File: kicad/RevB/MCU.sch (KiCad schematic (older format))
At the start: 12 parts, among them SW1 SW_SPDT, SW2 SW_SPST, U2 SE8233X2, U3 STM32F051K4Tx

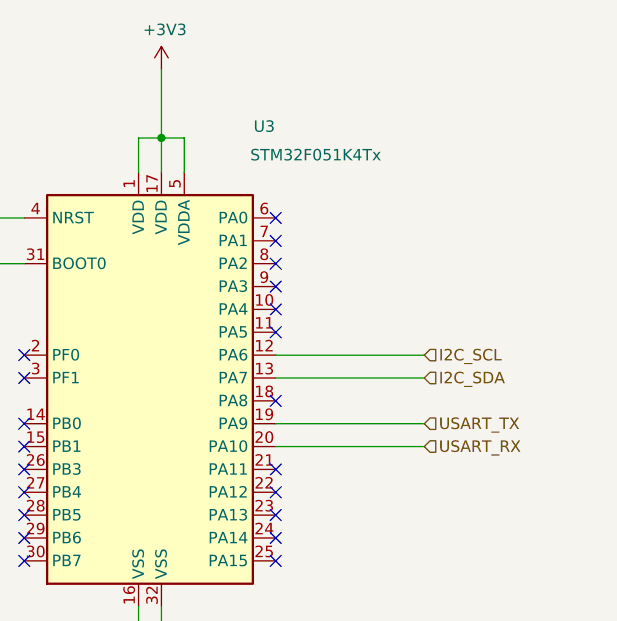
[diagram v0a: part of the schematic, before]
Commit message: updated revb hw
- Added pull up resistors to i2C bus (allows direct connection to mcu from oled port)
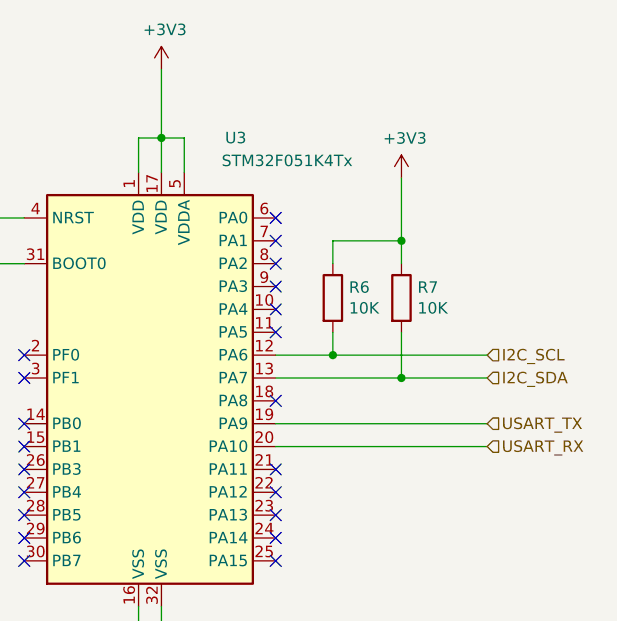
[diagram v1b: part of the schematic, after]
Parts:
- added R6, R7: 10K, Resistor_SMD:R_0805_2012Metric_Pad1.15x1.40mm_HandSolder, symbol Device:R
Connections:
- net +3V3: now also R6.1, R7.1
- net I2C_SCL: now also R6.2
- net I2C_SDA: now also R7.2
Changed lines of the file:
@@
 $EndDescr
 Wire Wire Line
-	7800 3725 8450 3725
-Wire Wire Line
-	7800 3625 8450 3625
-Wire Wire Line
-	7800 3325 8450 3325
-Wire Wire Line
-	7800 3425 8450 3425
+	7800 3725 8725 3725
+Wire Wire Line
+	7800 3625 8725 3625
+Wire Wire Line
+	7800 3325 8050 3325
+Wire Wire Line
+	7800 3425 8350 3425
 NoConn ~ 7800 3525
 NoConn ~ 7800 3225
@@
 NoConn ~ 7800 3925
 NoConn ~ 7800 4225
-Text HLabel 8450 3325 2    50   Input ~ 0
+Text HLabel 8725 3325 2    50   Input ~ 0
 I2C_SCL
-Text HLabel 8450 3425 2    50   Input ~ 0
+Text HLabel 8725 3425 2    50   Input ~ 0
 I2C_SDA
-Text HLabel 8450 3625 2    50   Input ~ 0
+Text HLabel 8725 3625 2    50   Input ~ 0
 USART_TX
-Text HLabel 8450 3725 2    50   Input ~ 0
+Text HLabel 8725 3725 2    50   Input ~ 0
 USART_RX
 $Comp
@@
 AR Path="/5F6E45CF" Ref="U?"  Part="1"
 AR Path="/5F6E342E/5F6E45CF" Ref="U3"  Part="1"
-F 0 "U3" H 7750 4525 50  0000 C CNN
-F 1 "STM32F051K4Tx" H 7975 4400 50  0000 C CNN
+F 0 "U3" H 7625 4475 50  0000 C CNN
+F 1 "STM32F051K4Tx" H 7850 4375 50  0000 C CNN
 F 2 "Package_QFP:LQFP-32_7x7mm_P0.8mm" H 6800 2525 50  0001 R CNN
 F 3 "http://www.st.com/st-web-ui/static/active/en/resource/technical/document/datasheet/DM00039193.pdf" H 7300 3425 50  0001 C CNN
@@
 Text Notes 5550 2175 0    50   ~ 0
 Tactile SPST salvaged\nfrom an old nano clone
+$Comp
+L Device:R R6
+U 1 1 5F70F57E
+P 8050 3075
+F 0 "R6" H 8120 3121 50  0000 L CNN
+F 1 "10K" H 8120 3030 50  0000 L CNN
+F 2 "Resistor_SMD:R_0805_2012Metric_Pad1.15x1.40mm_HandSolder" V 7980 3075 50  0001 C CNN
+F 3 "~" H 8050 3075 50  0001 C CNN
+	1    8050 3075
+	1    0    0    -1
+$EndComp
+$Comp
+L Device:R R7
+U 1 1 5F70FAD9
+P 8350 3075
+F 0 "R7" H 8420 3121 50  0000 L CNN
+F 1 "10K" H 8420 3030 50  0000 L CNN
+F 2 "Resistor_SMD:R_0805_2012Metric_Pad1.15x1.40mm_HandSolder" V 8280 3075 50  0001 C CNN
+F 3 "~" H 8350 3075 50  0001 C CNN
+	1    8350 3075
+	1    0    0    -1
+$EndComp
+$Comp
+L power:+3V3 #PWR?
+U 1 1 5F711644
+P 8350 2550
+AR Path="/5F711644" Ref="#PWR?"  Part="1"
+AR Path="/5F6E342E/5F711644" Ref="#PWR021"  Part="1"
+F 0 "#PWR021" H 8350 2400 50  0001 C CNN
+F 1 "+3V3" H 8365 2723 50  0000 C CNN
+F 2 "" H 8350 2550 50  0001 C CNN
+F 3 "" H 8350 2550 50  0001 C CNN
+	1    8350 2550
+	1    0    0    -1
+$EndComp
+Wire Wire Line
+	8350 2550 8350 2825
+Wire Wire Line
+	8350 2825 8050 2825
+Wire Wire Line
+	8050 2825 8050 2925
+Connection ~ 8350 2825
+Wire Wire Line
+	8350 2825 8350 2925
+Wire Wire Line
+	8050 3225 8050 3325
+Connection ~ 8050 3325
+Wire Wire Line
+	8050 3325 8725 3325
+Wire Wire Line
+	8350 3225 8350 3425
+Connection ~ 8350 3425
+Wire Wire Line
+	8350 3425 8725 3425
 $EndSCHEMATC

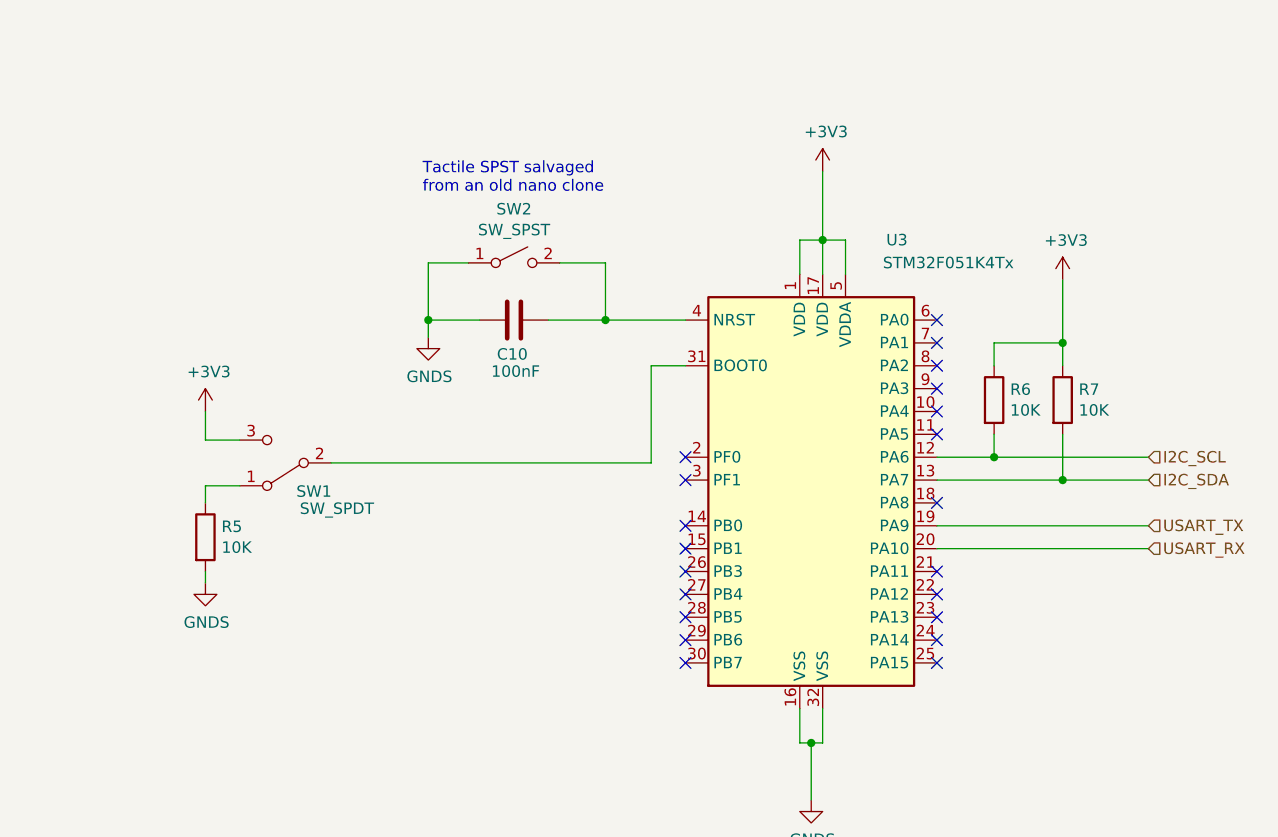
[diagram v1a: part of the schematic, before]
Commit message: updated hw
- corrected i2c pins
- changed reset btn to horizontal mount
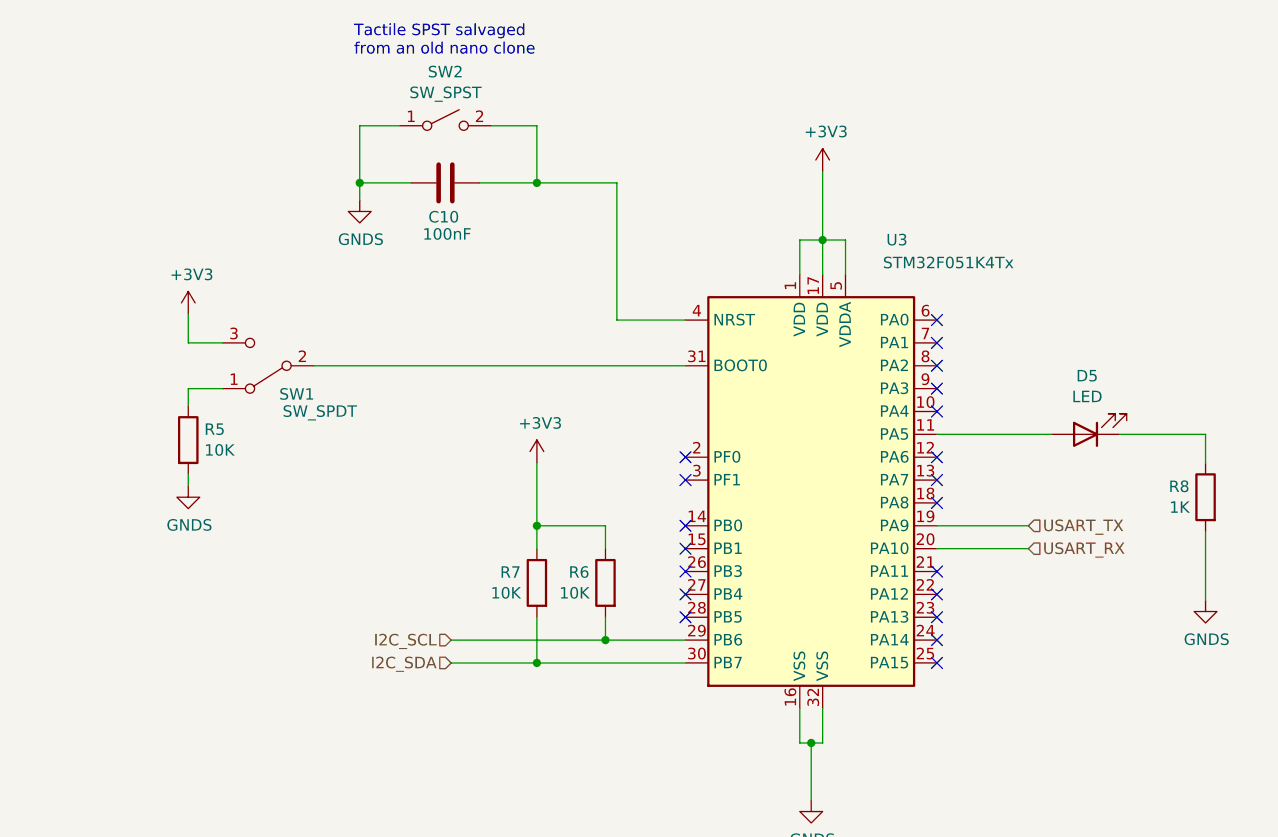
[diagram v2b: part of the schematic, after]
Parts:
- added D5: LED, LED_SMD:LED_0805_2012Metric_Pad1.15x1.40mm_HandSolder, symbol Device:LED
- added R8: 1K, Resistor_SMD:R_0805_2012Metric_Pad1.15x1.40mm_HandSolder, symbol Device:R
- SW2: footprint Button_Switch_SMD:SW_DIP_SPSTx01_Slide_6.7x4.1mm_W6.73mm_P2.54mm_LowProfile_JPin -> Button_Switch_SMD:Panasonic_EVQPUK_EVQPUB
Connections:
- net GNDS: now also R8.2
- net I2C_SCL: now also U3.29 (PB6); no longer U3.12 (PA6)
- net I2C_SDA: now also U3.30 (PB7); no longer U3.13 (PA7)
- net at U3.11 (PA5): now also D5.2 (A)
- new net: D5.1 (K), R8.1
- no-connect marks 21 -> 20
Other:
- moved on the sheet: C10, R5, R6, R7, SW1, SW2
